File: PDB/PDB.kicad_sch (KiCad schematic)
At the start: 33 parts, among them J2 ESC - XT90x4, J3 FC - XT30x1, J4 Sensors - XT30x1, J5 Jetson - XT60x1, J6 UART OUT, J7 Micro_SD_Card, U2 STM32H742VGTx

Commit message: added or battery input and temp sensing
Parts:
- added C29, C30: 1.5uF, Capacitor_SMD:C_1206_3216Metric, symbol Device:C
- added C31: 470nF, Capacitor_SMD:C_1206_3216Metric, symbol Device:C
- added D10, D12, D13, D9: SMAJ64A, Diode_SMD:D_SMA, symbol Diode:SMAJ64A
- added D11, D14: DDZ9699T 12V, symbol Device:D_Zener
- added Q5, Q7: IPT012N08N5, Package_TO_SOT_SMD:SOT-23, symbol Transistor_FET:2N7002E
- added Q6, Q8: BSC093N15NS5, Package_TO_SOT_SMD:SOT-23, symbol Transistor_FET:2N7002E
- added R24, R25, R28, R30: 100k, Resistor_SMD:R_0603_1608Metric_Pad0.98x0.95mm_HandSolder, symbol Device:R
- added R26, R29: 1k, Resistor_SMD:R_0603_1608Metric_Pad0.98x0.95mm_HandSolder, symbol Device:R
- added R31, R32, R33, R34, R35, R36: 10k, Resistor_SMD:R_0603_1608Metric_Pad0.98x0.95mm_HandSolder, symbol Device:R
- added U10, U11: LTC4359-DCB, Package_DFN_QFN:DFN-6-1EP_3x2mm_P0.5mm_EP1.65x1.35mm, symbol Power_Management:LTC4359-DCB
- added U13, U14, U15: MCP9804_DFN, Package_DFN_QFN:DFN-8-1EP_3x2mm_P0.5mm_EP1.7x1.4mm, symbol Sensor_Temperature:MCP9804_DFN
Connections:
- net +3.3V: now also R31.1, R32.1, R33.1, R34.1, R35.1, R36.1, U13.8 (V_{DD}), U14.7 (A0), U14.8 (V_{DD}), U15.6 (A1), U15.8 (V_{DD})
- net +BATT: now also C29.1, C30.1, Q6.3 (D), Q8.3 (D), U10.1 (OUT), U11.1 (OUT)
- net GND: now also C29.2, C30.2, C31.2, D10.1 (A1), D13.1 (A1), R26.2, R29.2, U10.7 (Pad), U11.7 (Pad), U13.4 (GND), U13.5 (A2), U13.6 (A1), U13.7 (A0), U13.9 (EP/GND), U14.4 (GND), U14.5 (A2), U14.6 (A1), U14.9 (EP/GND), U15.4 (GND), U15.5 (A2), U15.7 (A0), U15.9 (EP/GND)
- new net: R29.1, U11.6 (Vss)
- new net: D10.2 (A2), D9.2 (A2)
- new net: D11.1 (K), Q5.1 (G), Q6.1 (G), U10.2 (GATE)
- new net: D11.2 (A), Q5.2 (S), Q6.2 (S), R25.1, U10.3 (SRC)
- new net: R25.2, U10.4 (IN)
- new net: R24.2, U10.5 (~{SHDN})
- new net: R26.1, U10.6 (Vss)
- new net: C31.1, D14.1 (K), Q7.1 (G), Q8.1 (G), U11.2 (GATE)
- new net: D14.2 (A), Q7.2 (S), Q8.2 (S), R30.1, U11.3 (SRC)
- new net: R28.2, U11.5 (~{SHDN})
- new net: D12.2 (A2), D13.2 (A2)
- new net: R30.2, U11.4 (IN)
- new net SCL: R32.2, R33.2, R35.2, U13.2 (SCL), U14.2 (SCL), U15.2 (SCL)
- new net SDA: R31.2, R34.2, R36.2, U13.1 (SDA), U14.1 (SDA), U15.1 (SDA)
- new net batt_in: D12.1 (A1), D9.1 (A1), Q5.3 (D), Q7.3 (D), R24.1, R28.1
- no-connect marks 44 -> 47
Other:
- note added: "compute rail"
- note added: "input mosfets"
- note added: "power area"
- moved on the sheet: J2, J3, J4, J5, J6, J7, R19, R20, R21, R22, R23

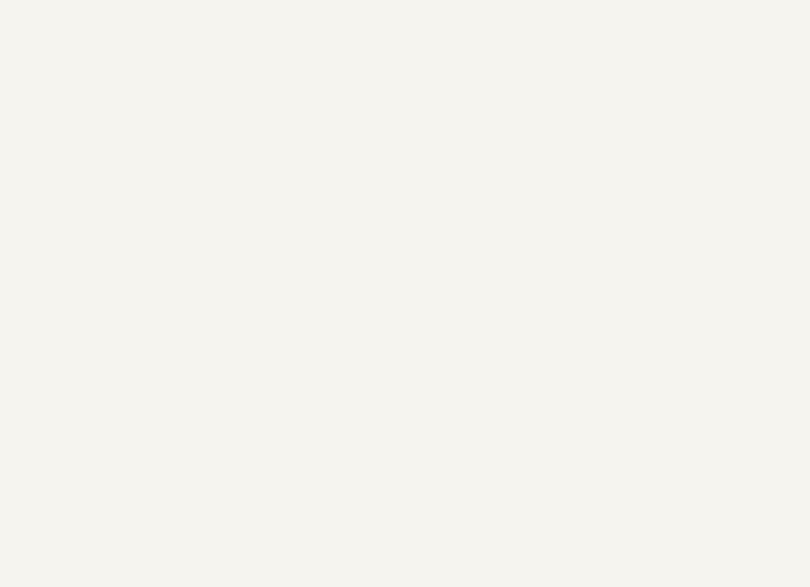
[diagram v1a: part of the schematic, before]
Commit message: added fuses to each
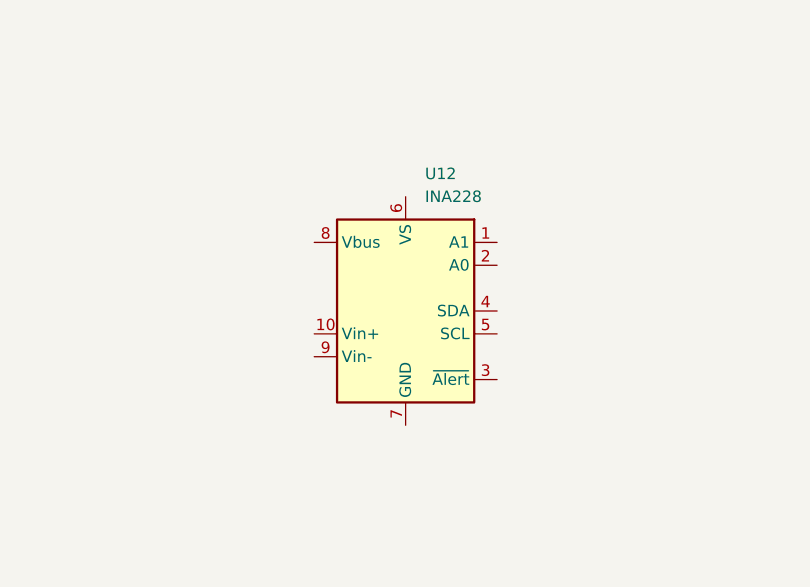
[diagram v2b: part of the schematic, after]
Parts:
- added U12: INA228, Package_SO:TSSOP-10_3x3mm_P0.5mm, symbol Sensor_Energy:INA228
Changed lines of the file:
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@@
+	)
+	(symbol
+		(lib_id "Sensor_Energy:INA228")
+		(at 344.17 224.79 0)
+		(unit 1)
+		(body_style 1)
+		(exclude_from_sim no)
+		(in_bom yes)
+		(on_board yes)
+		(in_pos_files yes)
+		(dnp no)
+		(fields_autoplaced yes)
+		(property "Reference" "U12"
+			(at 346.3133 209.55 0)
+			(show_name no)
+			(do_not_autoplace no)
+			(effects
+				(font
+					(size 1.27 1.27)
+				)
+				(justify left)
+			)
+		)
+		(property "Value" "INA228"
+			(at 346.3133 212.09 0)
+			(show_name no)
+			(do_not_autoplace no)
+			(effects
+				(font
+					(size 1.27 1.27)
+				)
+				(justify left)
+			)
+		)
+		(property "Footprint" "Package_SO:TSSOP-10_3x3mm_P0.5mm"
+			(at 364.49 236.22 0)
+			(hide yes)
+			(show_name no)
+			(do_not_autoplace no)
+			(effects
+				(font
+					(size 1.27 1.27)
+				)
+			)
+		)
+		(property "Datasheet" "https://www.ti.com/lit/ds/symlink/ina228.pdf"
+			(at 353.06 227.33 0)
+			(hide yes)
+			(show_name no)
+			(do_not_autoplace no)
+			(effects
+				(font
+					(size 1.27 1.27)
+				)
+			)
+		)
+		(property "Description" "High-Side or Low-Side Measurement, Bi-Directional Current and Power Monitor (0-85V) with I2C, SMBus-, and PMBus-Compatible Interface, TSSOP-10 (Texas DGS0010A / VSSOP)"
+			(at 344.17 224.79 0)
+			(hide yes)
+			(show_name no)
+			(do_not_autoplace no)
+			(effects
+				(font
+					(size 1.27 1.27)
+				)
+			)
+		)
+		(pin "1"
+		)
+		(pin "3"
+		)
+		(pin "4"
+		)
+		(pin "5"
+		)
+		(pin "2"
+		)
+		(pin "7"
+		)
+		(pin "6"
+		)
+		(pin "9"
+		)
+		(pin "10"
+		)
+		(pin "8"
+		)
+		(instances
+			(project "PDB"
+				(path "/a9cf05c4-aac5-4cf1-b700-1d3045f8dfbd"
+					(reference "U12")
+					(unit 1)
+				)
+			)
+		)
 	)
 	(symbol

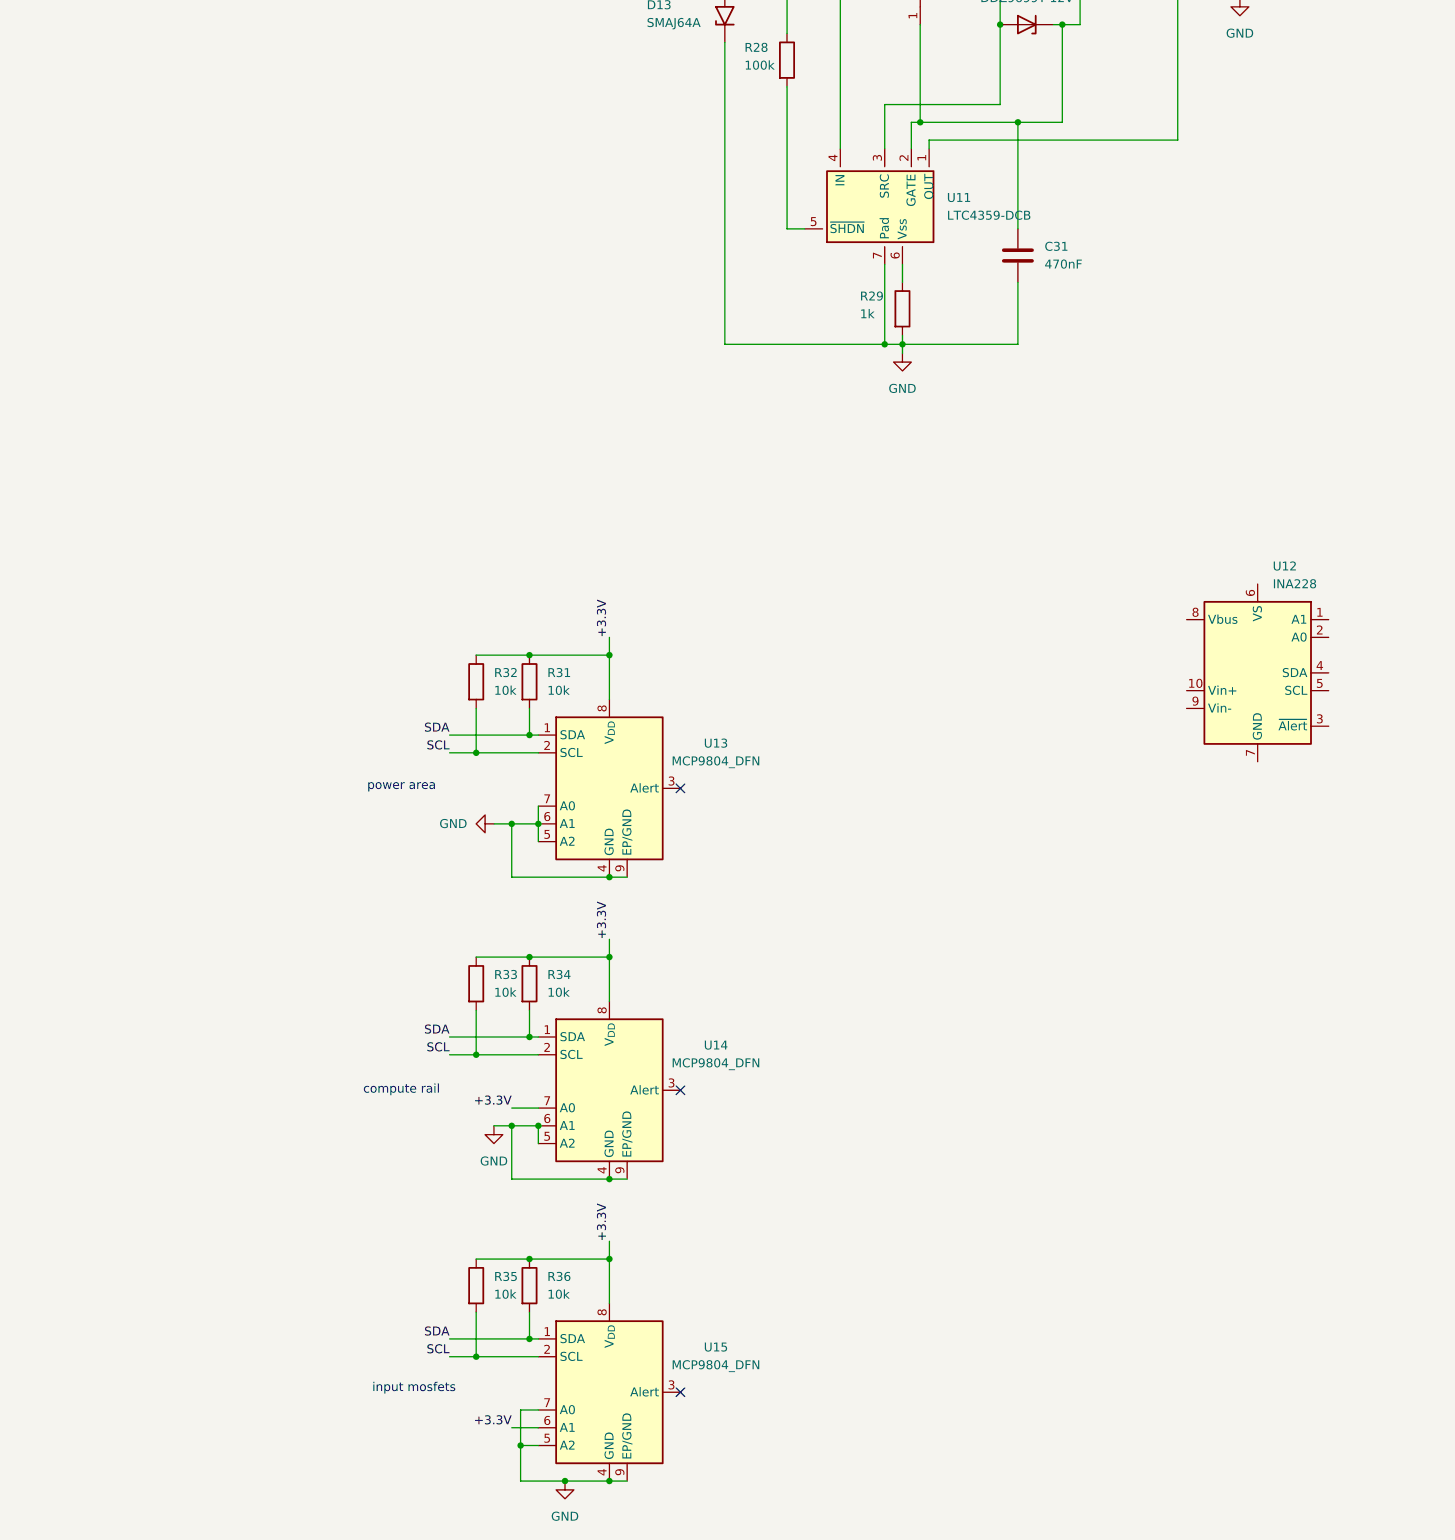
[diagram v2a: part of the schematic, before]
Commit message: added temp sensing on every rail available
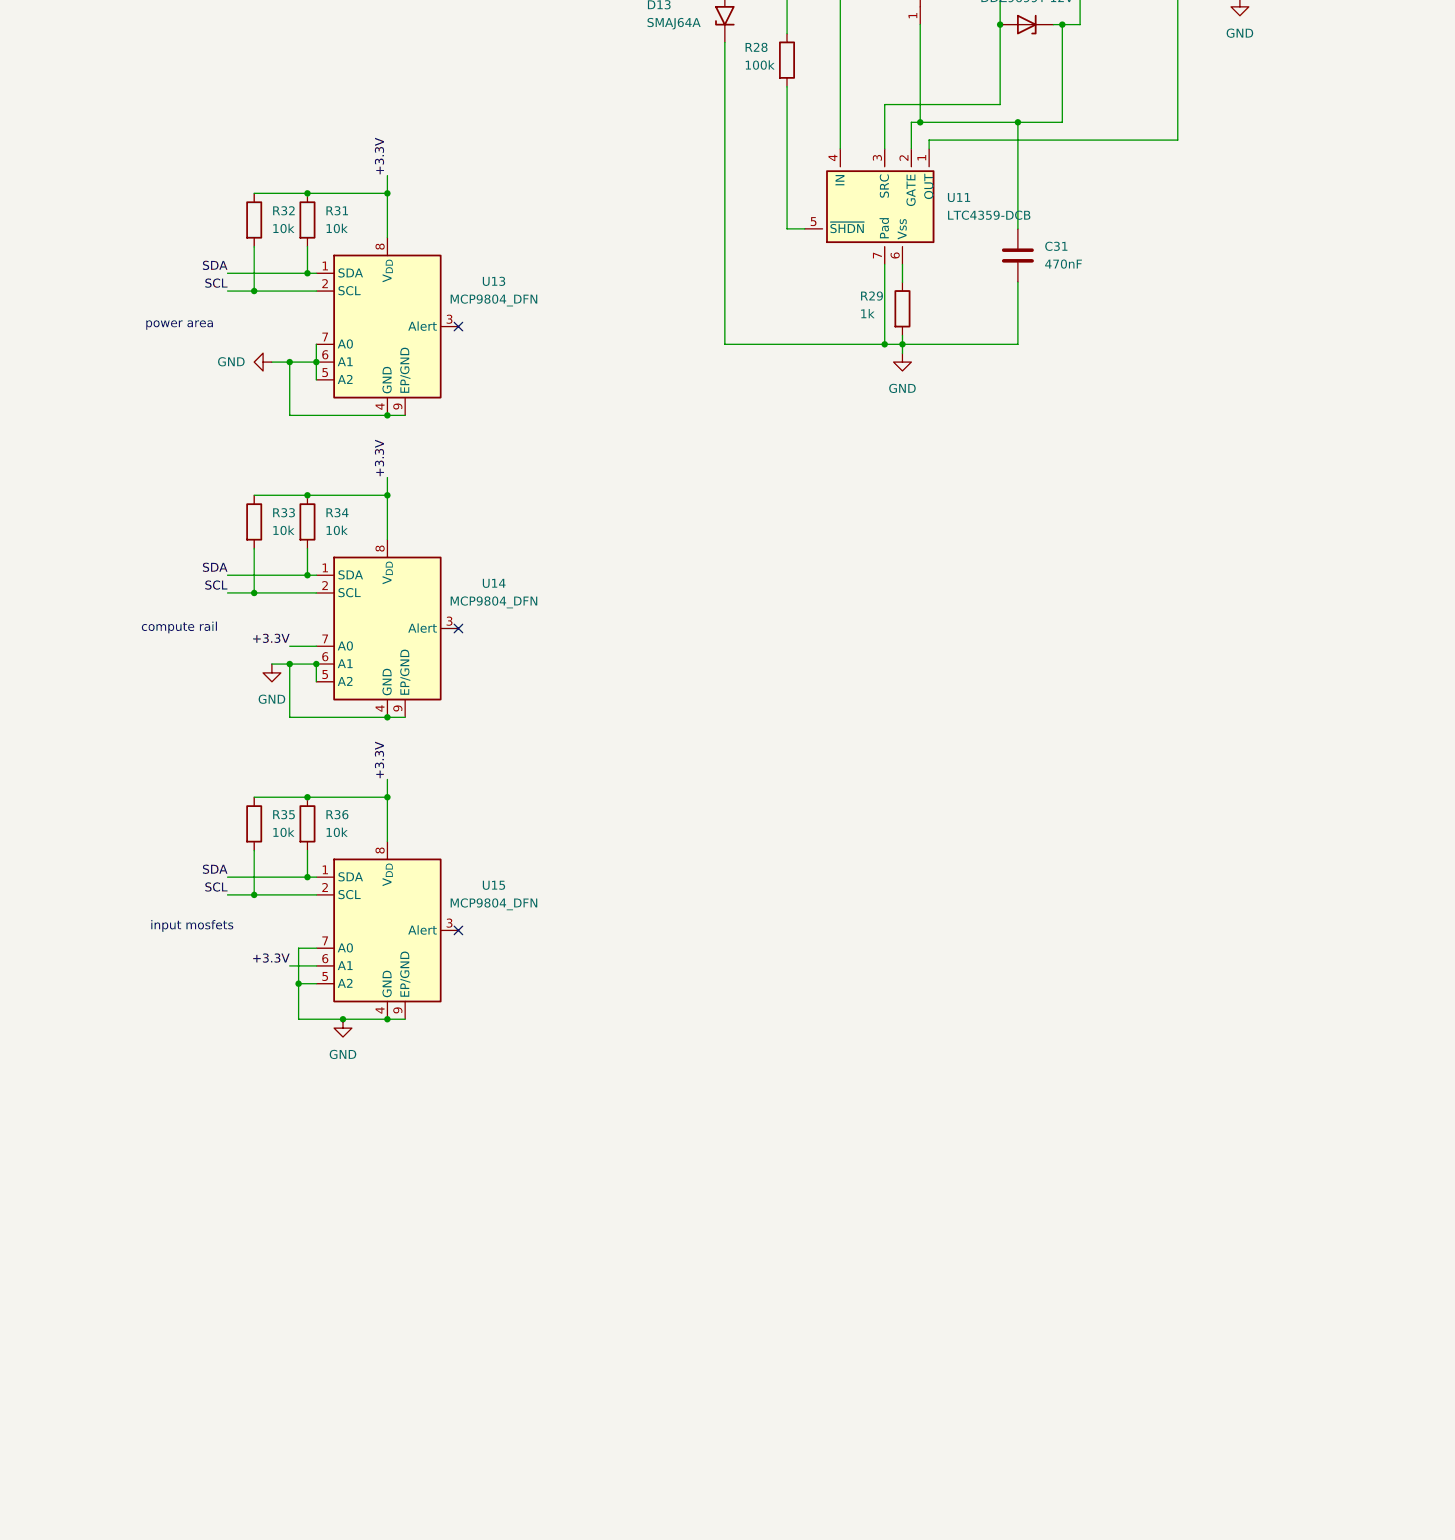
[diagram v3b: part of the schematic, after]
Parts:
- removed U12: INA228, Package_SO:TSSOP-10_3x3mm_P0.5mm, symbol Sensor_Energy:INA228
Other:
- moved on the sheet: R31, R32, R33, R34, R35, R36, U13, U14, U15
